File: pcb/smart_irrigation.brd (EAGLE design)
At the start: 100 x 80 mm, 13 parts, among them IC1 7805DT, IC2 7833DT, J1 1X2-3.5MM

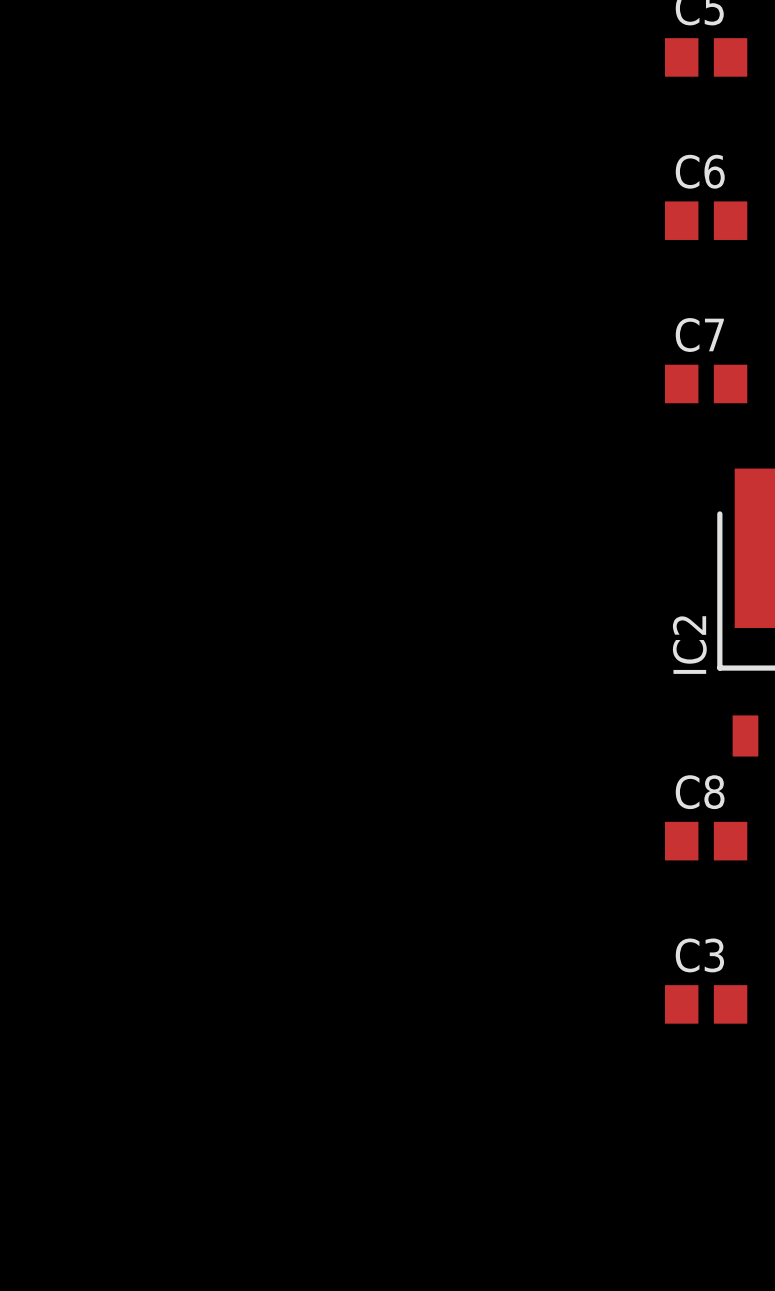
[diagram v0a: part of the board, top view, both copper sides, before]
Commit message: Add BL600 with autorun jumper to PCB
The autorun jumper is used to enable and disable the autorun feature of
the BL600.
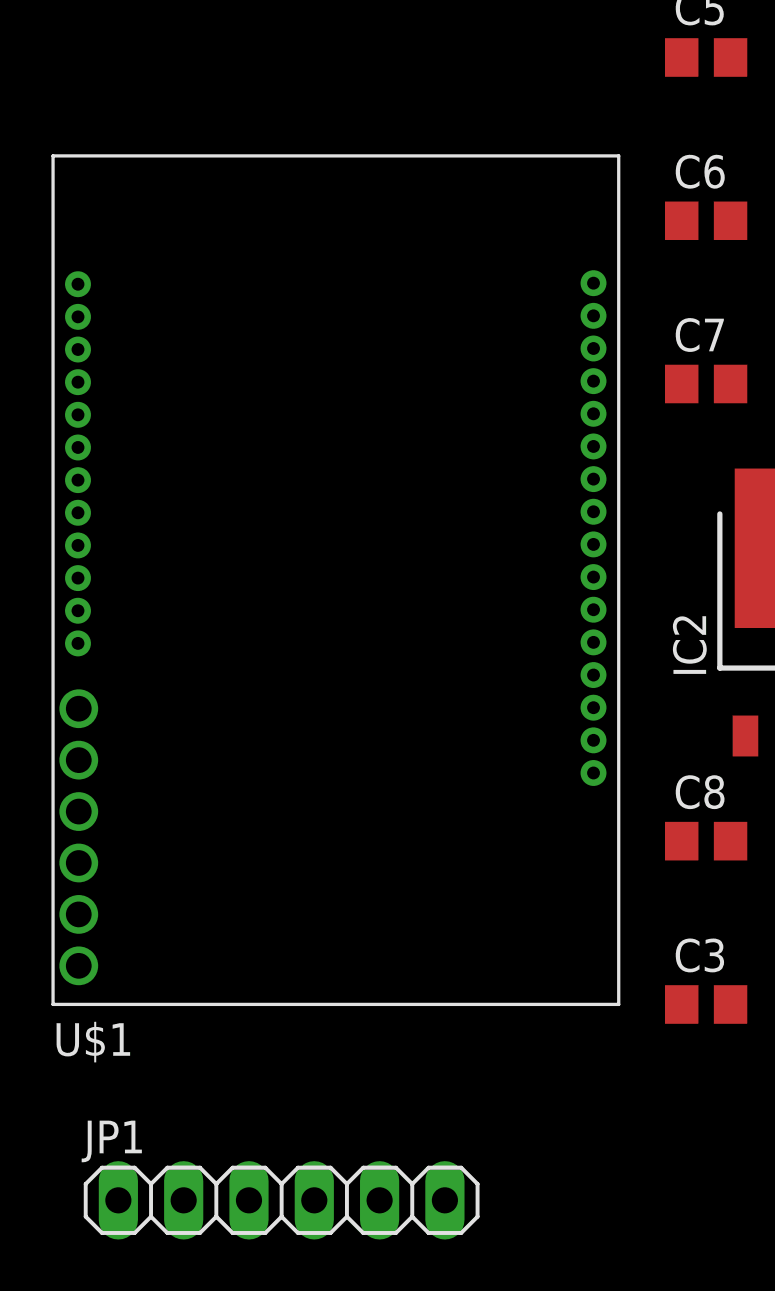
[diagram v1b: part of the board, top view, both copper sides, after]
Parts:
- added JP1: (no value), pinhead:1X06
- added U$1: BL600, library:BOB
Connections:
- removed net +3.3V: C10.1, C3.1, IC2.2
- new net +3V3: C10.1, C3.1, IC2.2, JP1.3, JP1.6, U$1.J5_3, U$1.J5_6
- new net N$2: JP1.2, U$1.J5_2
- new net N$5: JP1.5, U$1.J5_5
- net GND: now also JP1.1, JP1.4, U$1.11, U$1.28, U$1.29, U$1.J5_1, U$1.J5_4
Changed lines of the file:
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@@
 <element name="C9" library="rcl" package="C0805" value="10uF" x="-22.86" y="-87.63"/>
 <element name="C10" library="rcl" package="C0805" value="0.1uF" x="-21.59" y="-81.28"/>
+<element name="U$1" library="library" package="BOB" value="BL600" x="-44.45" y="-71.12"/>
+<element name="JP1" library="pinhead" package="1X06" value="" x="-45.72" y="-95.25"/>
 </elements>
 <signals>
@@
 <contactref element="C9" pad="2"/>
 <contactref element="C10" pad="2"/>
+<contactref element="U$1" pad="29"/>
+<contactref element="U$1" pad="28"/>
+<contactref element="U$1" pad="11"/>
+<contactref element="U$1" pad="J5_1"/>
+<contactref element="JP1" pad="1"/>
+<contactref element="JP1" pad="4"/>
+<contactref element="U$1" pad="J5_4"/>
+<wire x1="-44.45" y1="-95.25" x2="-52.07" y2="-95.25" width="0" layer="19" extent="1-1"/>
+<wire x1="-53.61" y1="-82.13" x2="-52.07" y2="-95.25" width="0" layer="19" extent="1-1"/>
+<wire x1="-53.61" y1="-76.13" x2="-53.61" y2="-82.13" width="0" layer="19" extent="1-1"/>
+<wire x1="-53.64" y1="-59.62" x2="-53.61" y2="-76.13" width="0" layer="19" extent="1-1"/>
+<wire x1="-28.26" y1="-87.63" x2="-44.45" y2="-95.25" width="0" layer="19" extent="1-1"/>
 <wire x1="-28.26" y1="-81.28" x2="-28.26" y2="-87.63" width="0" layer="19" extent="1-1"/>
+<wire x1="-33.59" y1="-78.63" x2="-28.26" y2="-81.28" width="0" layer="19" extent="1-1"/>
 <wire x1="-21.91" y1="-87.63" x2="-28.26" y2="-87.63" width="0" layer="19" extent="1-1"/>
 <wire x1="-20.64" y1="-81.28" x2="-21.91" y2="-87.63" width="0" layer="19" extent="1-1"/>
@@
 <wire x1="-28.26" y1="-63.5" x2="-25.4" y2="-69.89" width="0" layer="19" extent="1-1"/>
 <wire x1="-28.26" y1="-57.15" x2="-28.26" y2="-63.5" width="0" layer="19" extent="1-1"/>
+<wire x1="-33.59" y1="-59.58" x2="-28.26" y2="-57.15" width="0" layer="19" extent="1-1"/>
 <wire x1="-28.26" y1="-50.8" x2="-28.26" y2="-57.15" width="0" layer="19" extent="1-1"/>
 <wire x1="-16.83" y1="-69.85" x2="-25.4" y2="-69.89" width="0" layer="19" extent="1-1"/>
@@
 <wire x1="-4.07" y1="1.55" x2="-30.16" y2="-25.4" width="0" layer="19" extent="1-1"/>
 </signal>
-<signal name="+3.3V">
+<signal name="+3V3">
 <contactref element="IC2" pad="2"/>
 <contactref element="C3" pad="1"/>
 <contactref element="C10" pad="1"/>
+<contactref element="JP1" pad="3"/>
+<contactref element="U$1" pad="J5_3"/>
+<contactref element="JP1" pad="6"/>
+<contactref element="U$1" pad="J5_6"/>
+<wire x1="-39.37" y1="-95.25" x2="-46.99" y2="-95.25" width="0" layer="19" extent="1-1"/>
+<wire x1="-53.61" y1="-86.13" x2="-46.99" y2="-95.25" width="0" layer="19" extent="1-1"/>
+<wire x1="-53.61" y1="-80.13" x2="-53.61" y2="-86.13" width="0" layer="19" extent="1-1"/>
+<wire x1="-30.16" y1="-87.63" x2="-39.37" y2="-95.25" width="0" layer="19" extent="1-1"/>
 <wire x1="-22.54" y1="-81.28" x2="-30.16" y2="-87.63" width="0" layer="19" extent="1-1"/>
 <wire x1="-23.12" y1="-77.19" x2="-22.54" y2="-81.28" width="0" layer="19" extent="1-1"/>
 </signal>
+<signal name="N$2">
+<contactref element="JP1" pad="2"/>
+<contactref element="U$1" pad="J5_2"/>
+<wire x1="-53.61" y1="-78.13" x2="-49.53" y2="-95.25" width="0" layer="19" extent="1-1"/>
+</signal>
+<signal name="N$5">
+<contactref element="JP1" pad="5"/>
+<contactref element="U$1" pad="J5_5"/>
+<wire x1="-41.91" y1="-95.25" x2="-53.61" y2="-84.13" width="0" layer="19" extent="1-1"/>
+</signal>
 </signals>

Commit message: Rename EAGLE library file
Schematic and board files updated to use new library filename
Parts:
- IC2: device library:TO252 -> smart_irrigation:TO252
- U$1: device library:BOB -> smart_irrigation:BOB
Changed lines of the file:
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@@
 <element name="C6" library="rcl" package="C0805" value="10uF" x="-29.21" y="-57.15"/>
 <element name="C7" library="rcl" package="C0805" value="0.1uF" x="-29.21" y="-63.5"/>
-<element name="IC2" library="library" package="TO252" value="7833DT" x="-25.4" y="-72.39"/>
+<element name="IC2" library="smart_irrigation" package="TO252" value="7833DT" x="-25.4" y="-72.39"/>
 <element name="C3" library="rcl" package="C0805" value="10uF" x="-29.21" y="-87.63"/>
 <element name="C4" library="rcl" package="C0805" value="0.1uF" x="-17.78" y="-69.85"/>
@@
 <element name="C9" library="rcl" package="C0805" value="10uF" x="-22.86" y="-87.63"/>
 <element name="C10" library="rcl" package="C0805" value="0.1uF" x="-21.59" y="-81.28"/>
-<element name="U$1" library="library" package="BOB" value="BL600" x="-44.45" y="-71.12"/>
+<element name="U$1" library="smart_irrigation" package="BOB" value="BL600" x="-44.45" y="-71.12"/>
 <element name="JP1" library="pinhead" package="1X06" value="" x="-45.72" y="-95.25"/>
 </elements>

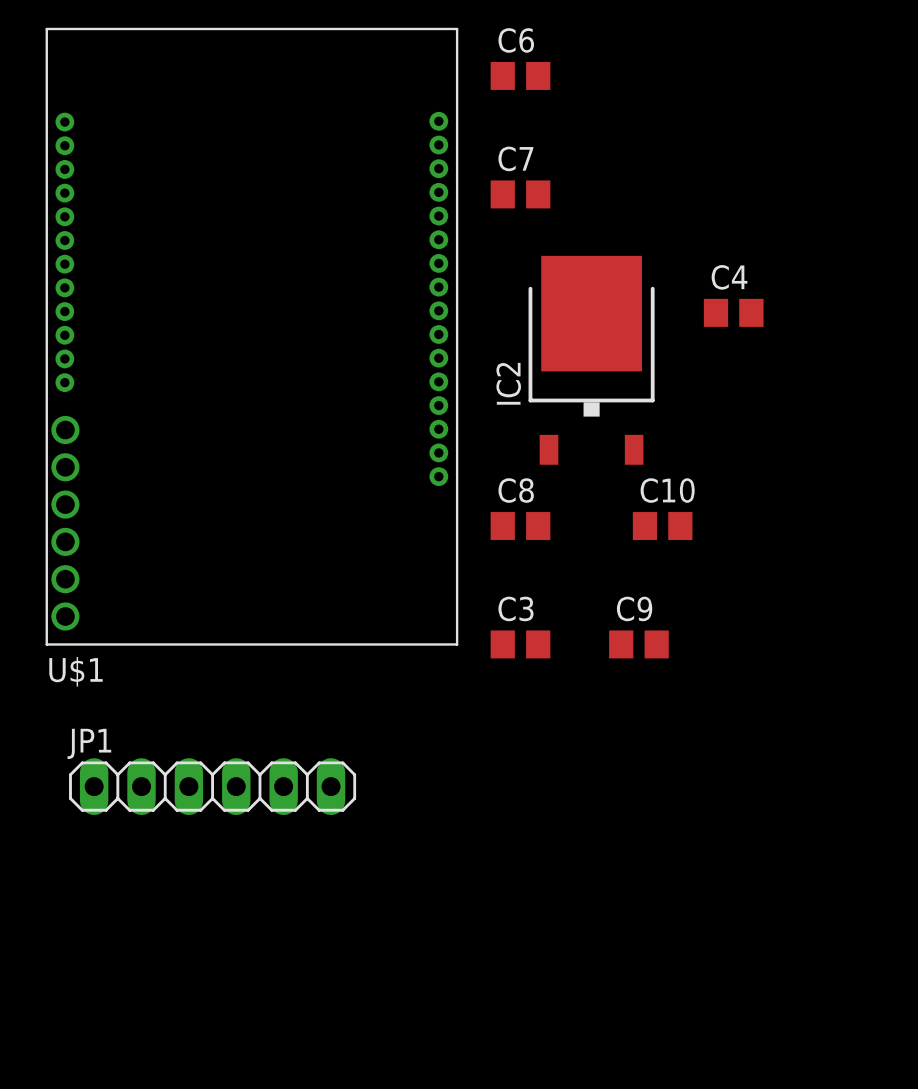
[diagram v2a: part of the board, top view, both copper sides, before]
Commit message: PCB: Add external headers
Having the breakout board pins run to external headers allows for both
debugging and adding additional peripherals if needed.
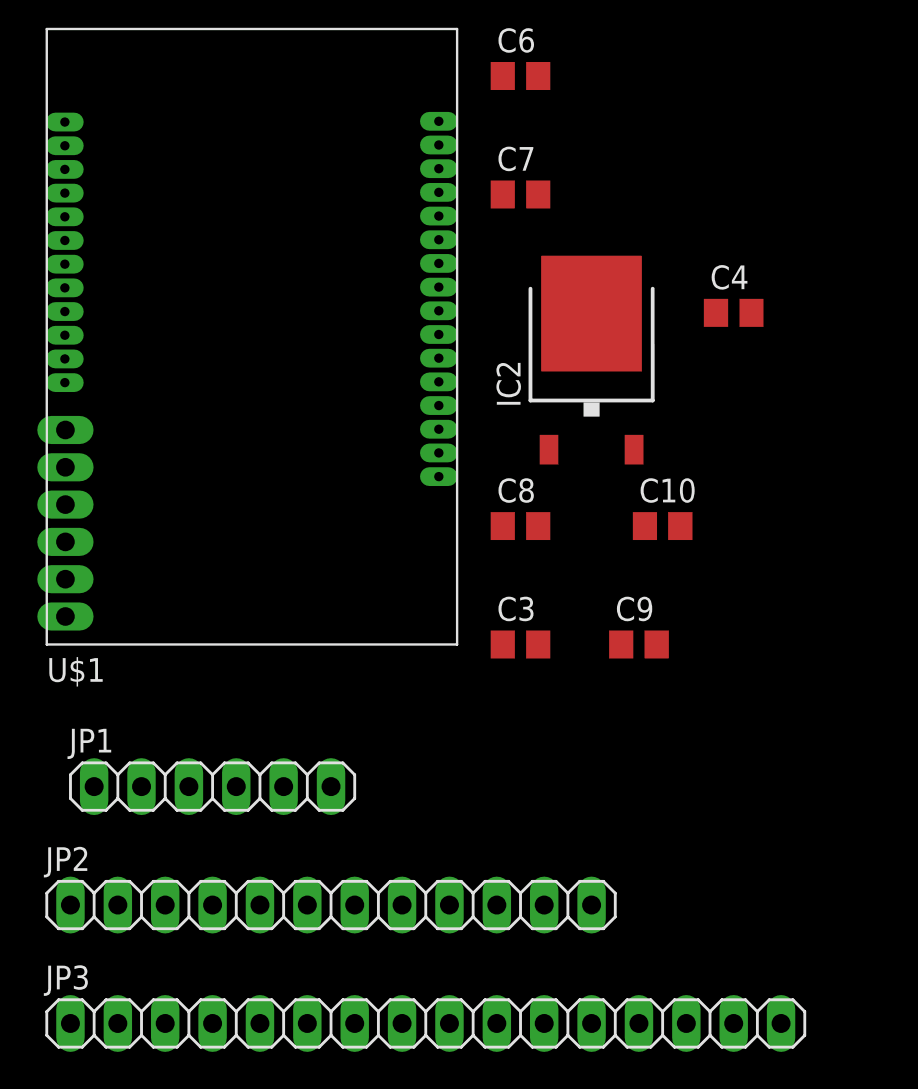
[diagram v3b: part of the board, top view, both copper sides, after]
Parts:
- added JP2: (no value), pinhead:1X12
- added JP3: (no value), pinhead:1X16
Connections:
- new net N$10: JP2.8, U$1.4
- new net N$11: JP2.9, U$1.5
- new net N$12: JP2.10, U$1.6
- new net N$13: JP2.11, U$1.7
- new net N$14: JP2.12, U$1.8
- new net N$16: JP3.2, U$1.27
- new net N$17: JP3.3, U$1.26
- new net N$18: JP3.4, U$1.25
- new net N$19: JP3.5, U$1.24
- new net N$20: JP3.6, U$1.22
- new net N$21: JP3.7, U$1.21
- new net N$22: JP3.8, U$1.20
- new net N$23: JP3.9, U$1.19
- new net N$24: JP3.10, U$1.18
- new net N$25: JP3.11, U$1.16
- new net N$26: JP3.12, U$1.15
- new net N$27: JP3.13, U$1.14
- new net N$28: JP3.14, U$1.13
- new net N$29: JP3.15, U$1.12
- new net N$4: JP2.2, U$1.36
- new net N$5: JP2.3, U$1.38
- new net N$6: JP2.4, U$1.39
- new net N$7: JP2.5, U$1.41
- new net N$8: JP2.6, U$1.42
- new net N$9: JP2.7, U$1.2
- net GND: now also JP2.1, JP3.1, JP3.16
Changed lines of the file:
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@@
 <element name="U$1" library="smart_irrigation" package="BOB" value="BL600" x="-44.45" y="-71.12"/>
 <element name="JP1" library="pinhead" package="1X06" value="" x="-45.72" y="-95.25"/>
+<element name="JP2" library="pinhead" package="1X12" value="" x="-39.37" y="-101.6"/>
+<element name="JP3" library="pinhead" package="1X16" value="" x="-34.29" y="-107.95"/>
 </elements>
 <signals>
@@
 <contactref element="C9" pad="2"/>
 <contactref element="C10" pad="2"/>
-<contactref element="U$1" pad="29"/>
-<contactref element="U$1" pad="28"/>
-<contactref element="U$1" pad="11"/>
-<contactref element="U$1" pad="J5_1"/>
 <contactref element="JP1" pad="1"/>
 <contactref element="JP1" pad="4"/>
+<contactref element="U$1" pad="J5_1"/>
 <contactref element="U$1" pad="J5_4"/>
+<contactref element="JP3" pad="16"/>
+<contactref element="U$1" pad="11"/>
+<contactref element="U$1" pad="28"/>
+<contactref element="JP3" pad="1"/>
+<contactref element="U$1" pad="29"/>
+<contactref element="JP2" pad="1"/>
+<wire x1="-53.34" y1="-101.6" x2="-53.34" y2="-107.95" width="0" layer="19" extent="1-1"/>
+<wire x1="-52.07" y1="-95.25" x2="-53.34" y2="-101.6" width="0" layer="19" extent="1-1"/>
 <wire x1="-44.45" y1="-95.25" x2="-52.07" y2="-95.25" width="0" layer="19" extent="1-1"/>
 <wire x1="-53.61" y1="-82.13" x2="-52.07" y2="-95.25" width="0" layer="19" extent="1-1"/>
@@
 <wire x1="-28.26" y1="-25.4" x2="-28.26" y2="-31.75" width="0" layer="19" extent="1-1"/>
 <wire x1="-26.14" y1="-17.78" x2="-28.26" y2="-25.4" width="0" layer="19" extent="1-1"/>
+<wire x1="-15.24" y1="-107.95" x2="-21.91" y2="-87.63" width="0" layer="19" extent="1-1"/>
 <wire x1="-6.35" y1="8.85" x2="-26.14" y2="-17.78" width="0" layer="19" extent="1-1"/>
 </signal>
@@
 <contactref element="C10" pad="1"/>
 <contactref element="JP1" pad="3"/>
+<contactref element="JP1" pad="6"/>
 <contactref element="U$1" pad="J5_3"/>
-<contactref element="JP1" pad="6"/>
 <contactref element="U$1" pad="J5_6"/>
 <wire x1="-39.37" y1="-95.25" x2="-46.99" y2="-95.25" width="0" layer="19" extent="1-1"/>
@@
 <wire x1="-23.12" y1="-77.19" x2="-22.54" y2="-81.28" width="0" layer="19" extent="1-1"/>
 </signal>
+<signal name="N$1">
+<contactref element="U$1" pad="J5_2"/>
+<contactref element="JP1" pad="2"/>
+<wire x1="-53.61" y1="-78.13" x2="-49.53" y2="-95.25" width="0" layer="19" extent="1-1"/>
+</signal>
 <signal name="N$2">
-<contactref element="JP1" pad="2"/>
-<contactref element="U$1" pad="J5_2"/>
-<wire x1="-53.61" y1="-78.13" x2="-49.53" y2="-95.25" width="0" layer="19" extent="1-1"/>
+<contactref element="U$1" pad="J5_5"/>
+<contactref element="JP1" pad="5"/>
+<wire x1="-41.91" y1="-95.25" x2="-53.61" y2="-84.13" width="0" layer="19" extent="1-1"/>
+</signal>
+<signal name="N$4">
+<contactref element="JP2" pad="2"/>
+<contactref element="U$1" pad="36"/>
+<wire x1="-53.64" y1="-60.89" x2="-50.8" y2="-101.6" width="0" layer="19" extent="1-1"/>
 </signal>
 <signal name="N$5">
-<contactref element="JP1" pad="5"/>
-<contactref element="U$1" pad="J5_5"/>
-<wire x1="-41.91" y1="-95.25" x2="-53.61" y2="-84.13" width="0" layer="19" extent="1-1"/>
+<contactref element="U$1" pad="38"/>
+<contactref element="JP2" pad="3"/>
+<wire x1="-53.64" y1="-62.16" x2="-48.26" y2="-101.6" width="0" layer="19" extent="1-1"/>
+</signal>
+<signal name="N$6">
+<contactref element="JP2" pad="4"/>
+<contactref element="U$1" pad="39"/>
+<wire x1="-53.64" y1="-63.43" x2="-45.72" y2="-101.6" width="0" layer="19" extent="1-1"/>
+</signal>
+<signal name="N$7">
+<contactref element="U$1" pad="41"/>
+<contactref element="JP2" pad="5"/>
+<wire x1="-53.64" y1="-64.7" x2="-43.18" y2="-101.6" width="0" layer="19" extent="1-1"/>
+</signal>
+<signal name="N$8">
+<contactref element="JP2" pad="6"/>
+<contactref element="U$1" pad="42"/>
+<wire x1="-53.64" y1="-65.97" x2="-40.64" y2="-101.6" width="0" layer="19" extent="1-1"/>
+</signal>
+<signal name="N$9">
+<contactref element="JP2" pad="7"/>
+<contactref element="U$1" pad="2"/>
+<wire x1="-53.64" y1="-67.24" x2="-38.1" y2="-101.6" width="0" layer="19" extent="1-1"/>
+</signal>
+<signal name="N$10">
+<contactref element="U$1" pad="4"/>
+<contactref element="JP2" pad="8"/>
+<wire x1="-53.64" y1="-68.51" x2="-35.56" y2="-101.6" width="0" layer="19" extent="1-1"/>
+</signal>
+<signal name="N$11">
+<contactref element="JP2" pad="9"/>
+<contactref element="U$1" pad="5"/>
+<wire x1="-53.64" y1="-69.78" x2="-33.02" y2="-101.6" width="0" layer="19" extent="1-1"/>
+</signal>
+<signal name="N$12">
+<contactref element="U$1" pad="6"/>
+<contactref element="JP2" pad="10"/>
+<wire x1="-53.64" y1="-71.05" x2="-30.48" y2="-101.6" width="0" layer="19" extent="1-1"/>
+</signal>
+<signal name="N$13">
+<contactref element="JP2" pad="11"/>
+<contactref element="U$1" pad="7"/>
+<wire x1="-53.64" y1="-72.32" x2="-27.94" y2="-101.6" width="0" layer="19" extent="1-1"/>
+</signal>
+<signal name="N$14">
+<contactref element="U$1" pad="8"/>
+<contactref element="JP2" pad="12"/>
+<wire x1="-53.64" y1="-73.59" x2="-25.4" y2="-101.6" width="0" layer="19" extent="1-1"/>
+</signal>
+<signal name="N$16">
+<contactref element="JP3" pad="2"/>
+<contactref element="U$1" pad="27"/>
+<wire x1="-33.59" y1="-60.85" x2="-50.8" y2="-107.95" width="0" layer="19" extent="1-1"/>
+</signal>
+<signal name="N$17">
+<contactref element="U$1" pad="26"/>
+<contactref element="JP3" pad="3"/>
+<wire x1="-33.59" y1="-62.12" x2="-48.26" y2="-107.95" width="0" layer="19" extent="1-1"/>
+</signal>
+<signal name="N$18">
+<contactref element="JP3" pad="4"/>
+<contactref element="U$1" pad="25"/>
+<wire x1="-33.59" y1="-63.39" x2="-45.72" y2="-107.95" width="0" layer="19" extent="1-1"/>
+</signal>
+<signal name="N$19">
+<contactref element="U$1" pad="24"/>
+<contactref element="JP3" pad="5"/>
+<wire x1="-33.59" y1="-64.66" x2="-43.18" y2="-107.95" width="0" layer="19" extent="1-1"/>
+</signal>
+<signal name="N$20">
+<contactref element="JP3" pad="6"/>
+<contactref element="U$1" pad="22"/>
+<wire x1="-33.59" y1="-65.93" x2="-40.64" y2="-107.95" width="0" layer="19" extent="1-1"/>
+</signal>
+<signal name="N$21">
+<contactref element="U$1" pad="21"/>
+<contactref element="JP3" pad="7"/>
+<wire x1="-33.59" y1="-67.2" x2="-38.1" y2="-107.95" width="0" layer="19" extent="1-1"/>
+</signal>
+<signal name="N$22">
+<contactref element="JP3" pad="8"/>
+<contactref element="U$1" pad="20"/>
+<wire x1="-33.59" y1="-68.47" x2="-35.56" y2="-107.95" width="0" layer="19" extent="1-1"/>
+</signal>
+<signal name="N$23">
+<contactref element="U$1" pad="19"/>
+<contactref element="JP3" pad="9"/>
+<wire x1="-33.59" y1="-69.74" x2="-33.02" y2="-107.95" width="0" layer="19" extent="1-1"/>
+</signal>
+<signal name="N$24">
+<contactref element="JP3" pad="10"/>
+<contactref element="U$1" pad="18"/>
+<wire x1="-33.59" y1="-71.01" x2="-30.48" y2="-107.95" width="0" layer="19" extent="1-1"/>
+</signal>
+<signal name="N$25">
+<contactref element="U$1" pad="16"/>
+<contactref element="JP3" pad="11"/>
+<wire x1="-33.59" y1="-72.28" x2="-27.94" y2="-107.95" width="0" layer="19" extent="1-1"/>
+</signal>
+<signal name="N$26">
+<contactref element="JP3" pad="12"/>
+<contactref element="U$1" pad="15"/>
+<wire x1="-33.59" y1="-73.55" x2="-25.4" y2="-107.95" width="0" layer="19" extent="1-1"/>
+</signal>
+<signal name="N$27">
+<contactref element="U$1" pad="14"/>
+<contactref element="JP3" pad="13"/>
+<wire x1="-33.59" y1="-74.82" x2="-22.86" y2="-107.95" width="0" layer="19" extent="1-1"/>
+</signal>
+<signal name="N$28">
+<contactref element="JP3" pad="14"/>
+<contactref element="U$1" pad="13"/>
+<wire x1="-33.59" y1="-76.09" x2="-20.32" y2="-107.95" width="0" layer="19" extent="1-1"/>
+</signal>
+<signal name="N$29">
+<contactref element="U$1" pad="12"/>
+<contactref element="JP3" pad="15"/>
+<wire x1="-33.59" y1="-77.36" x2="-17.78" y2="-107.95" width="0" layer="19" extent="1-1"/>
 </signal>
 </signals>
